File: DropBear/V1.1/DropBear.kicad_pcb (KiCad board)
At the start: 2 copper layers, 116.5 x 98 mm, 191 parts, among them IC1 MAX9926UAEE_V+, IC2 ZXMS6006DT8, IC3 ZXMS6006DT8, IC4 ZXMS6006DT8, J1 Delphi_Sicma_24, J2 Delphi_Sicma_24, J3 EBC05DRXN, J4 Conn_01x04, Q1 Q_PNP_BCEC, Q2 Q_DUAL_NMOS_S1G1D2S2G2D1, Q3 Q_DUAL_NMOS_S1G1D2S2G2D1, SW1 SW_DPDT_x2, SW2 SW_DPDT_x2, SW3 SW_DPDT_x2, SW4 SW_DIP_x02, SW5 SW_DPDT_x2, U1 Teensy3.5, U10 SP720, U11 74AHC1G32, U12 TC4424A, U13 LMV324LIDT, U14 W25Q32JVSS, U18 KP234, U19 MCP2562-E-SN, U2 MC33814, U20 LMV324LIDT, U3 TC4424A, U4 TC4424A, U5 MC33810, U6 MC33810, U7 TC4424A, U8 TC4424A, U9 ADXL343

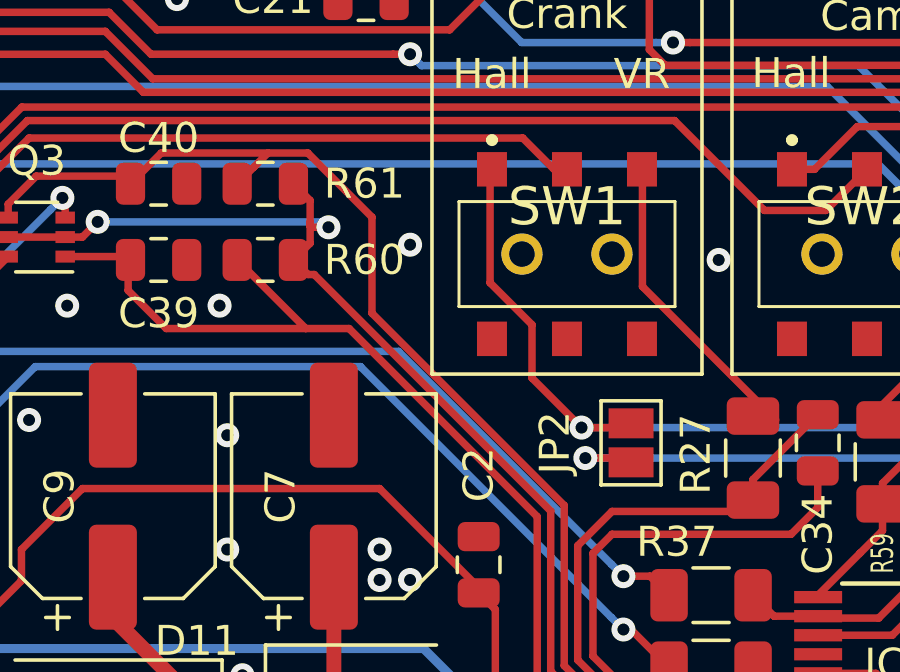
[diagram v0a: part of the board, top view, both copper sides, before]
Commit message: Fix for unconnected ground on 1 capacitor
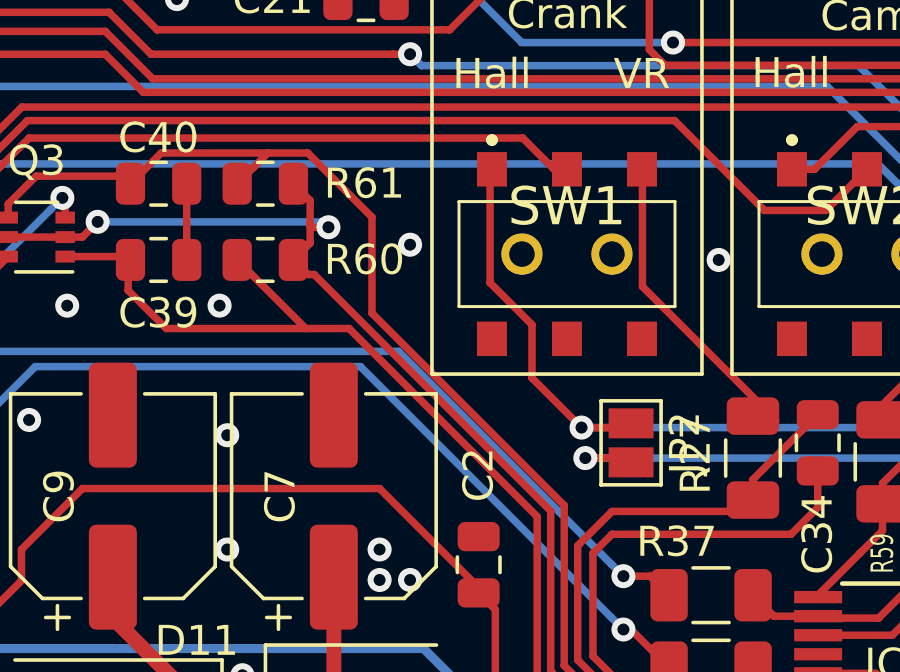
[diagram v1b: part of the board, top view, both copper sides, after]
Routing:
- net GND: track 92.3 -> 94.9 mm
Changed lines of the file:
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@@
   )
   (setup
+    (stackup
+      (layer "F.SilkS" (type "Top Silk Screen"))
+      (layer "F.Paste" (type "Top Solder Paste"))
+      (layer "F.Mask" (type "Top Solder Mask") (thickness 0.01))
+      (layer "F.Cu" (type "copper") (thickness 0.035))
+      (layer "dielectric 1" (type "core") (thickness 1.51) (material "FR4") (epsilon_r 4.5) (loss_tangent 0.02))
+      (layer "B.Cu" (type "copper") (thickness 0.035))
+      (layer "B.Mask" (type "Bottom Solder Mask") (thickness 0.01))
+      (layer "B.Paste" (type "Bottom Solder Paste"))
+      (layer "B.SilkS" (type "Bottom Silk Screen"))
+      (copper_finish "None")
+      (dielectric_constraints no)
+    )
     (pad_to_mask_clearance 0.051)
     (solder_mask_min_width 0.25)
@@
     (at 208 108.5)
     (zone_connect 2)
-    (attr smd)
+    (attr smd allow_soldermask_bridges)
     (fp_text reference "U5" (at 0.026 -6.646) (layer "F.SilkS")
         (effects (font (size 1.94495 1.94495) (thickness 0.05)))
@@
     (descr "SOT-363, SC-70-6")
     (tags "SOT-363 SC-70-6")
-    (attr smd)
+    (attr smd allow_soldermask_bridges)
     (fp_text reference "Q2" (at 3 0) (layer "F.SilkS")
         (effects (font (size 1 1) (thickness 0.15)))
@@
     (descr "LQFP, 48 Pin (http://www.analog.com/media/en/technical-documentation/data-sheets/LTC7810.pdf), generated with kicad-footprint-generator ipc_qfp_generator.py")
     (tags "LQFP QFP")
-    (attr smd)
-    (fp_text reference "U2" (at 0 -5.85 270) (layer "F.SilkS")
+    (attr smd allow_soldermask_bridges)
+    (fp_text reference "U2" (at 0 -5.85 90) (layer "F.SilkS")
         (effects (font (size 1 1) (thickness 0.15)))
     )
-    (fp_text value "MC33814" (at 0 5.85 270) (layer "F.Fab")
+    (fp_text value "MC33814" (at 0 5.85 90) (layer "F.Fab")
         (effects (font (size 1 1) (thickness 0.15)))
     )
-    (fp_text user "${REFERENCE}" (at 0 0 270) (layer "F.Fab")
+    (fp_text user "${REFERENCE}" (at 0 0 90) (layer "F.Fab")
         (effects (font (size 1 1) (thickness 0.15)))
     )
@@
     (descr "16-Lead Plastic Shrink Small Outline Narrow Body (QR)-.150\" Body [QSOP] (see Microchip Packaging Specification 00000049BS.pdf)")
     (tags "SSOP 0.635")
-    (attr smd)
+    (attr smd allow_soldermask_bridges)
     (fp_text reference "IC1" (at 0 0) (layer "F.SilkS")
         (effects (font (size 1 1) (thickness 0.15)))
@@
     (descr "SOT-363, SC-70-6")
     (tags "SOT-363 SC-70-6")
-    (attr smd)
+    (attr smd allow_soldermask_bridges)
     (fp_text reference "Q3" (at 0 2.54) (layer "F.SilkS")
         (effects (font (size 1 1) (thickness 0.15)))
@@
     (descr "LGA, 14 Pin (http://www.st.com/resource/en/datasheet/lsm303dlhc.pdf), generated with kicad-footprint-generator ipc_noLead_generator.py")
     (tags "LGA NoLead")
-    (attr smd)
+    (attr smd allow_soldermask_bridges)
     (fp_text reference "U9" (at 2.54 0 90) (layer "F.SilkS")
         (effects (font (size 1 1) (thickness 0.15)))
@@
     (descr "SOT-353, SC-70-5")
     (tags "SOT-353 SC-70-5")
-    (attr smd)
+    (attr smd allow_soldermask_bridges)
     (fp_text reference "U11" (at 0 -2 90) (layer "F.SilkS")
         (effects (font (size 1 1) (thickness 0.15)))
     )
-    (fp_text value "74AHC1G32" (at 0 2 270) (layer "F.Fab")
+    (fp_text value "74AHC1G32" (at 0 2 90) (layer "F.Fab")
         (effects (font (size 1 1) (thickness 0.15)))
     )
@@
     (at 246.38 31.496 180)
     (descr "Infineon_PG-DSO-8-16")
-    (attr smd)
+    (attr smd allow_soldermask_bridges)
     (fp_text reference "U18" (at 1.016 3.302) (layer "F.SilkS")
         (effects (font (size 1 1) (thickness 0.15)))
@@
     (at 208 91.5)
     (zone_connect 2)
-    (attr smd)
+    (attr smd allow_soldermask_bridges)
     (fp_text reference "U6" (at 0 -7) (layer "F.SilkS")
         (effects (font (size 1.94495 1.94495) (thickness 0.05)))
@@
     (descr "SMD Solder Jumper, 1x1.5mm Pads, 0.3mm gap, open")
     (tags "solder jumper open")
-    (attr exclude_from_pos_files exclude_from_bom)
+    (attr exclude_from_pos_files exclude_from_bom allow_soldermask_bridges)
     (fp_text reference "JP1" (at 0.127 -1.778) (layer "F.SilkS")
         (effects (font (size 0.75 0.75) (thickness 0.15)))
@@
     (descr "SMD Solder Jumper, 1x1.5mm Pads, 0.3mm gap, open")
     (tags "solder jumper open")
-    (attr exclude_from_pos_files exclude_from_bom)
-    (fp_text reference "JP2" (at 0 2.54 90) (layer "F.SilkS")
+    (attr exclude_from_pos_files exclude_from_bom allow_soldermask_bridges)
+    (fp_text reference "JP2" (at 0 -1.8 90) (layer "F.SilkS")
         (effects (font (size 1 1) (thickness 0.15)))
     )
@@
     (descr "SMD Solder Jumper, 1x1.5mm Pads, 0.3mm gap, open")
     (tags "solder jumper open")
-    (attr exclude_from_pos_files exclude_from_bom)
+    (attr exclude_from_pos_files exclude_from_bom allow_soldermask_bridges)
     (fp_text reference "JP3" (at -3.048 0 90) (layer "F.SilkS")
         (effects (font (size 1 1) (thickness 0.15)))
@@
     (descr "SMD Solder Jumper, 1x1.5mm Pads, 0.3mm gap, open")
     (tags "solder jumper open")
-    (attr exclude_from_pos_files exclude_from_bom)
+    (attr exclude_from_pos_files exclude_from_bom allow_soldermask_bridges)
     (fp_text reference "JP4" (at 0 2.032) (layer "F.SilkS") hide
         (effects (font (size 1 1) (thickness 0.15)))
@@
   (segment (start 182.5475 89.5) (end 181.899 89.5) (width 0.25) (layer "F.Cu") (net 20))
   (segment (start 191.6625 74.25) (end 188.75 74.25) (width 0.25) (layer "F.Cu") (net 20))
+  (segment (start 184.3255 44.196) (end 184.3255 41.656) (width 0.25) (layer "F.Cu") (net 20))
   (segment (start 185.75 71.25) (end 187.5 73) (width 0.25) (layer "F.Cu") (net 20))
   (segment (start 207.299626 57.976) (end 208.118671 58.795045) (width 0.25) (layer "F.Cu") (net 20))

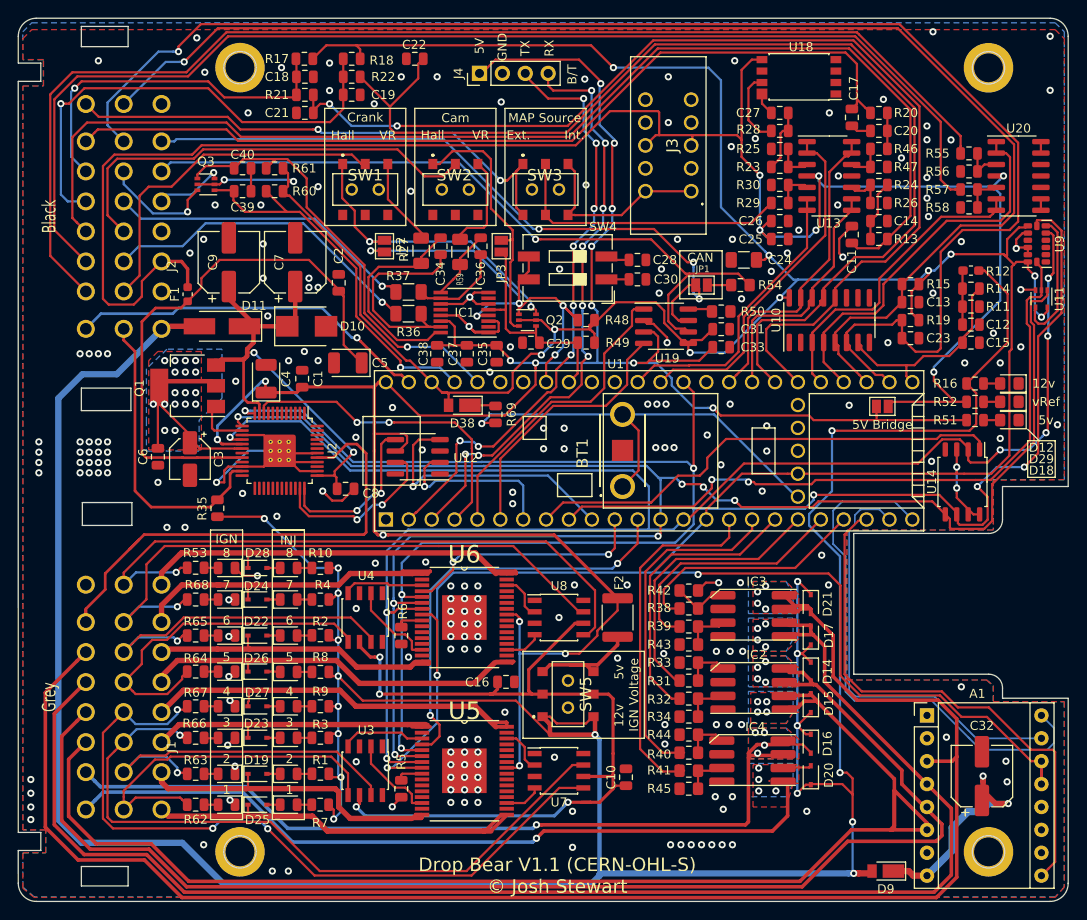
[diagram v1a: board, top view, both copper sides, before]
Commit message: Minor conversion corrections on Dropbear PCB
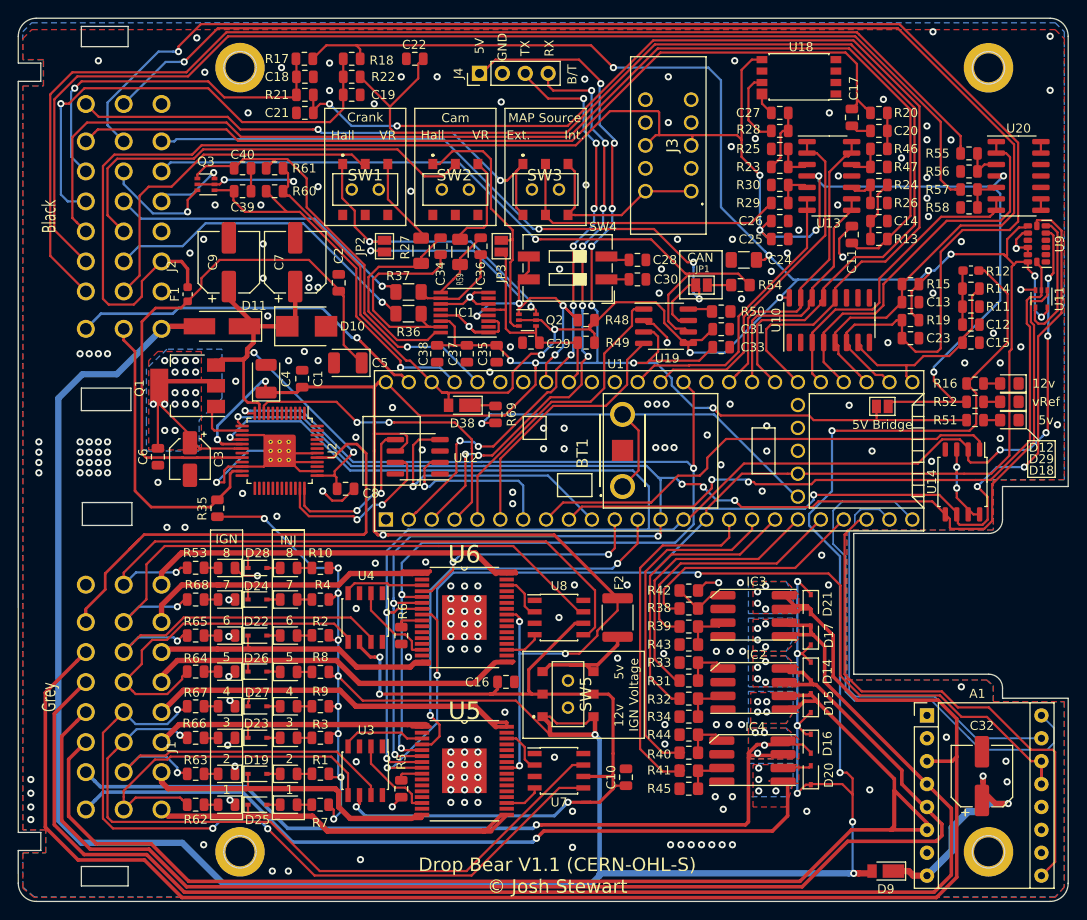
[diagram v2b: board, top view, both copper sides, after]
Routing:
- net GND: vias 220 -> 223
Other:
- board text added: "NOTE! PCB requires 2oz copper, do NOT use with 1oz"
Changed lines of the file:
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@@
       (net 68 "+3V3"))
     (pad "27" thru_hole circle (at 16.51 0) (size 1.6 1.6) (drill 1.1) (layers "*.Cu" "*.Mask")
-      (net 20 "GND"))
+      (net 20 "GND") (zone_connect 2))
     (pad "28" thru_hole circle (at 16.51 -2.54) (size 1.6 1.6) (drill 1.1) (layers "*.Cu" "*.Mask")
       (net 139 "PROG"))
@@
     (tags "resistor")
     (attr smd)
-    (fp_text reference "R27" (at -0.127 1.905 90) (layer "F.SilkS")
+    (fp_text reference "R27" (at -0.381 1.778 90) (layer "F.SilkS")
         (effects (font (size 1 1) (thickness 0.15)))
     )
@@
     (tags "solder jumper open")
     (attr exclude_from_pos_files exclude_from_bom allow_soldermask_bridges)
-    (fp_text reference "JP2" (at 0 -1.8 90) (layer "F.SilkS")
+    (fp_text reference "JP2" (at 0 2.667 90) (layer "F.SilkS")
         (effects (font (size 1 1) (thickness 0.15)))
     )
@@
   (gr_text "Edge length = 116.5mm (Incl curves)" (at 220 20.5) (layer "Cmts.User")
     (effects (font (size 1.5 1.5) (thickness 0.3)))
+  )
+  (gr_text "NOTE! PCB requires 2oz copper, do NOT use with 1oz" (at 216.027 127.254) (layer "Cmts.User")
+    (effects (font (size 2 2) (thickness 0.3)))
   )
   (via (at 263.144 99.187) (size 0.8) (drill 0.4) (layers "F.Cu" "B.Cu") (net 0))
@@
   (via (at 179.07 49.53) (size 0.8) (drill 0.4) (layers "F.Cu" "B.Cu") (net 20))
   (via (at 234.95 71.247) (size 0.8) (drill 0.4) (layers "F.Cu" "B.Cu") (net 20))
+  (via (at 252.984 110.617) (size 0.8) (drill 0.4) (layers "F.Cu" "B.Cu") (free) (net 20))
   (via (at 168.402 62.23) (size 0.8) (drill 0.4) (layers "F.Cu" "B.Cu") (net 20))
   (via (at 203.708 85.344) (size 0.8) (drill 0.4) (layers "F.Cu" "B.Cu") (net 20))
@@
   (via (at 187.198 80.264) (size 0.8) (drill 0.4) (layers "F.Cu" "B.Cu") (net 20))
   (via (at 180.5 76.5) (size 0.8) (drill 0.4) (layers "F.Cu" "B.Cu") (net 20))
+  (via (at 253.238 73.025) (size 0.8) (drill 0.4) (layers "F.Cu" "B.Cu") (free) (net 20))
   (via (at 267.462 63.246) (size 0.8) (drill 0.4) (layers "F.Cu" "B.Cu") (net 20))
   (via (at 243.84 51.054) (size 0.8) (drill 0.4) (layers "F.Cu" "B.Cu") (net 20))
@@
   (via (at 190.754 53.848) (size 0.8) (drill 0.4) (layers "F.Cu" "B.Cu") (net 20))
   (via (at 230.251 105.537) (size 0.8) (drill 0.4) (layers "F.Cu" "B.Cu") (net 20))
+  (via (at 196.469 118.364) (size 0.8) (drill 0.4) (layers "F.Cu" "B.Cu") (free) (net 20))
   (via (at 208.026 88.011) (size 0.8) (drill 0.4) (layers "F.Cu" "B.Cu") (net 20))
   (via (at 266.7 59.944) (size 0.8) (drill 0.4) (layers "F.Cu" "B.Cu") (net 20))
